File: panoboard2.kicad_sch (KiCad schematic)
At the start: 54 parts, among them J1 Conn_01x01, J10 Conn_01x01_Socket, J2 Conn_01x01_Socket, J3 Conn_01x01, J4 Conn_01x03, J5 I2C3, J7 Screw_Terminal_01x03, J8 Conn_01x08, J9 Conn_01x08_Pin, M1 Motor_AC, P1 Conn_WallPlug_Earth, P2 PCB_Patch, P3 PCB_Patch, SW1 SW_Push, SW2 SW_Push, U1 SRV05-4, U2 DS18B20, U8 OLED128X64

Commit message: More mods
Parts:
- added C1: 100n 250V, Capacitor_THT:C_Rect_L7.0mm_W6.0mm_P5.00mm, symbol Device:C
- added JP1, JP10, JP11, JP12, JP13, JP14, JP2, JP3, JP4, JP5, JP6, JP7, JP8, JP9: PCB_Pin_Breakout, TestPoint:TestPoint_Pad_1.0x1.0mm, symbol local:PCB_Pin_Breakout
- added M2: TINYPICO, TINYPICO:TINYPICO, symbol local:TINYPICO
- added R1: 22R 2W, Resistor_THT:R_Axial_DIN0207_L6.3mm_D2.5mm_P10.16mm_Horizontal, symbol Device:R
- added R3: 1k, Resistor_THT:R_Axial_DIN0207_L6.3mm_D2.5mm_P10.16mm_Horizontal, symbol Device:R
- added R4: 100k, Resistor_THT:R_Axial_DIN0207_L6.3mm_D2.5mm_P10.16mm_Horizontal, symbol Device:R
- J7: renamed from J8; value Conn_01x08 -> MOLEX 53375-0810
- RV1: renamed from RV3; value Varistor -> Varistor 10D271K
- U3: renamed from U1; now fitted
- renumbered D5 to D1, F3 to F2, J7 to J1, J4 to J2, J2 to J3, J10 to J4, J1 to J5, J3 to J6, J9 to J8, J5 to J9, JP9 to JP15, JP11 to JP16, JP13 to JP17, JP15 to JP18, JP17 to JP19, JP22 to JP20, JP24 to JP21, JP10 to JP22, JP12 to JP23, JP14 to JP24, JP16 to JP25, JP18 to JP26, JP20 to JP27, JP21 to JP28, JP23 to JP29, JP19 to JP30, JP1 to JP31, JP3 to JP32, JP5 to JP33, JP6 to JP34, JP8 to JP35, JP2 to JP36, JP4 to JP37, JP7 to JP38, R1 to R2, R24 to R5, U2 to U1, U8 to U2
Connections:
- net +3V3: now also U3.5 (VP), M2.7 (V3.3)
- net AC switcher 1/LOAD_A: now also C1.1
- net AC switcher 1/LOAD_N: now also R1.2
- net BUZZ1: now also JP27.1, U4.12 (A2CH0/TCH11/GPIO11), JP10.1, M2.14 (5), R3.2
- net BUZZ2: now also JP28.1, U4.14 (A2CH1/TCH12/GPIO12), JP11.1, M2.13 (18), R3.1, R4.2
- net DS18B20: now also U3.4 (IO3), JP4.1, M2.4 (15)
- net GND: now also U3.2 (VN), M2.9 (GND), R4.1
- net HEATER: now also U3.3 (IO2), JP3.1, M2.3 (27)
- net LED: now also JP19.1, U4.9 (A1CH8/TCH9/GPIO9), JP1.1, M2.1 (25)
- net MOTOR: now also U3.1 (IO1), JP2.1, M2.2 (26)
- net SCL: now also JP9.1, M2.15 (22)
- net SDA: now also JP8.1, M2.16 (21)
- net SW1: now also JP38.1, U4.20 (GPIO0), JP6.1, M2.6 (4); no longer JP27.1, U4.12 (A2CH0/TCH11/GPIO11)
- net SW2: now also JP26.1, U4.10 (A1CH9/TCH10/GPIO10), JP5.1, M2.5 (14); no longer JP28.1, U4.14 (A2CH1/TCH12/GPIO12)
- net THERM: now also U3.6 (IO4), JP14.1, M2.17 (32)
- net at M1.1: now also J8.8 (Pin_8); no longer J8.5 (Pin_5)
- net at M1.2: now also J8.5 (Pin_5); no longer J8.8 (Pin_8)
- net Earth: no longer names the net of J4.1 (Pin_1), P1.2 (AC_N)
- net Earth: no longer P1.3 (EARTH)
- new net: JP13.1, M2.11 (23)
- new net: JP12.1, M2.12 (19)
- new net: JP7.1, M2.18 (33)
- new net: C1.2, R1.1
- new net GNDPWR: P1.3 (EARTH)
- no-connect marks 7 -> 20
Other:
- sheet AC switcher renamed AC switcher 1
- sheet AC switcher1 renamed AC switcher 2
- note added: "Resistors are DNP"
- moved on the sheet: C2, J4, J6, J7, J8, M1, P2, P3, U4

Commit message: Revision 1.0c, after fit tests
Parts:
- removed JP10, JP11, JP12, JP13, JP14, JP15, JP16, JP17, JP18, JP19, JP2, JP20, JP21, JP26, JP27, JP28, JP3, JP35, JP36, JP37, JP38, JP4, JP5, JP6, JP7, JP8, JP9: PCB_Pin_Breakout, TestPoint:TestPoint_Pad_1.0x1.0mm, symbol local:PCB_Pin_Breakout
- added BZ2: FUET9018, Buzzer_Beeper:Buzzer_CUI_CPT-9019S-SMT, symbol Device:Buzzer
- added C3: 10n 1000V, Capacitor_THT:C_Rect_L18.0mm_W7.0mm_P15.00mm_FKS3_FKP3, symbol Device:C
- added C4: 10n, Capacitor_SMD:C_0805_2012Metric, symbol Device:C
- added D2: R LED, LED_SMD:LED_0805_2012Metric_Pad1.15x1.40mm_HandSolder, symbol Device:LED
- added D3: SS34, Diode_SMD:D_SMA, symbol Diode:SS34
- added H2: MountingHole, local:MountingHole, symbol local:MountingHole
- added J12: I2C2, Connector_PinHeader_2.54mm:PinHeader_1x04_P2.54mm_Vertical, symbol Connector_Generic:Conn_01x04
- added J4: Conn_01x01_Socket, symbol Connector:Conn_01x01_Socket
- added J7: WHT/HTR, TestPoint:TestPoint_Bridge_Pitch5.08mm_Drill1.3mm, symbol Connector_Generic:Conn_01x01
- added K1: Relay_SPDT, local:Relay_SPDT_SANYOU_SRD_Series_Form_C, symbol Relay:Relay_SPDT
- added Q1: 2N7000, Package_TO_SOT_THT:TO-92_Inline, symbol Transistor_FET:2N7000
- added Q2: BT136S-600, Package_TO_SOT_SMD:TO-252-2, symbol Triac_Thyristor:BT136-600
- added Q3: BT136-600, local:TO-220-3_Vertical, symbol Triac_Thyristor:BT136-600
- added R11: 220R, Resistor_SMD:R_0805_2012Metric, symbol Device:R
- added R12: 360R 1W, Resistor_THT:R_Axial_DIN0414_L11.9mm_D4.5mm_P15.24mm_Horizontal, symbol Device:R
- added R13: 360R, Resistor_THT:R_Axial_DIN0207_L6.3mm_D2.5mm_P10.16mm_Horizontal, symbol Device:R
- added R14: 10k, Resistor_SMD:R_0805_2012Metric, symbol Device:R
- added R4: 1k, Resistor_SMD:R_0805_2012Metric, symbol Device:R
- added R7: R so I=5mA, Resistor_SMD:R_0805_2012Metric, symbol Device:R
- added R8: R so I=10mA, Resistor_SMD:R_0805_2012Metric, symbol Device:R
- added R9: 39R 2W, Resistor_THT:R_Axial_DIN0617_L17.0mm_D6.0mm_P20.32mm_Horizontal, symbol Device:R
- added RV2, RV3, RV4, RV5: 10D271K, Varistor:RV_Disc_D12mm_W3.9mm_P7.5mm, symbol Device:Varistor
- added S1: JS1400BFQ, local:SW_JS1400BFQ, symbol local:JS1400BFQ
- added SW3, SW4, SW5: SW_Push, local:SW_Push_SPST_NO_432, symbol Switch:SW_Push
- added SW6: RotaryEncoder_Switch_MP, Rotary_Encoder:RotaryEncoder_Alps_EC11E-Switch_Vertical_H20mm, symbol Device:RotaryEncoder_Switch_MP
- added U6: MOC3063, Package_DIP:DIP-6_W7.62mm, symbol Relay_SolidState:MOC3063M
- added U7: MOC3063S, local:SOIC-6, symbol Relay_SolidState:MOC3063M
- BZ1: footprint (none) -> local:Buzzer_D12mm_H8.1mm; AliExpress (none) -> 1005006866915063; TODO (none) -> 1
- C1: footprint Capacitor_THT:C_Rect_L7.0mm_W6.0mm_P5.00mm -> Capacitor_THT:C_Rect_L9.0mm_W4.2mm_P7.50mm_MKT; AliExpress (none) -> 1005006719072774; TODO (none) -> 1
- C2: footprint Capacitor_THT:C_Rect_L41.5mm_W20.0mm_P37.50mm_MKS4 -> local:C_Rect_L24.0mm_W12.6mm_P20.00mm_MKT; AliExpress (none) -> 1005006292339527; TODO (none) -> 1
- D1: footprint (none) -> LED_SMD:LED_0805_2012Metric_Pad1.15x1.40mm_HandSolder; TODO (none) -> 1
- F2: value Fuse -> 5A; footprint (none) -> Fuse:Fuseholder_Cylinder-5x20mm_Stelvio-Kontek_PTF78_Horizontal_Open; AliExpress (none) -> 1005002077970716; TODO (none) -> ?
- H1: footprint ozhelm:MountingHole -> local:MountingHole
- J1: value Screw_Terminal_01x03 -> DS18B20; footprint (none) -> TerminalBlock_RND:TerminalBlock_RND_205-00046_1x03_P5.00mm_Horizontal; AliExpress (none) -> 32867118953
- J10: renamed from J8; value Conn_01x08_Pin -> MOTOR
- J11: renamed from J9; value I2C3 -> I2C1; symbol Connector_Generic:Conn_01x04 -> Connector_Generic_MountingPin:Conn_01x04_MountingPin; AliExpress (none) -> 1005005040794478; TODO (none) -> 1
- J2: value Conn_01x03 -> THERMISTOR; footprint (none) -> Connector_JST:JST_EH_B3B-EH-A_1x03_P2.50mm_Vertical; TODO (none) -> 1
- J3: AliExpress (none) -> 33040947135; TODO (none) -> 1
- J5: renamed from J4; AliExpress (none) -> 33040947135; TODO (none) -> 1
- J6: renamed from J5; value Conn_01x01 -> BLK/MAINS L; footprint (none) -> TestPoint:TestPoint_Bridge_Pitch5.08mm_Drill1.3mm; AliExpress (none) -> 1005005477459338; TODO (none) -> 1
- J8: renamed from J6; value Conn_01x01 -> ORA/MAINS N; footprint (none) -> TestPoint:TestPoint_Bridge_Pitch5.08mm_Drill1.3mm; AliExpress (none) -> 1005005477459338; TODO (none) -> 1
- J9: renamed from J7; footprint Connector_PinHeader_2.54mm:PinHeader_1x08_P2.54mm_Vertical -> local:MOLEX_533750810; AliExpress (none) -> 1005006639933927; TODO (none) -> ?
- M2: footprint TINYPICO:TINYPICO -> local:TINYPICO; TODO (none) -> 1
- P2, P3: footprint ozhelm:SolderJumper-2_P1.3mm_Bridged_Pad1.0x1.5mm -> local:SolderJumper-2_P1.3mm_Bridged_Pad1.0x1.5mm; TODO (none) -> 1
- PS1: value IRM-03-3.3 -> HLK-5M03; footprint Converter_ACDC:Converter_ACDC_MeanWell_IRM-03-xx_THT -> Converter_ACDC:Converter_ACDC_Hi-Link_HLK-5Mxx; symbol Converter_ACDC:IRM-03-3.3 -> Converter_ACDC:HLK-5M03; AliExpress (none) -> 1005006490570335; TODO (none) -> 1
- R2: renamed from R1; footprint Resistor_THT:R_Axial_DIN0207_L6.3mm_D2.5mm_P10.16mm_Horizontal -> local:R_Axial_DIN0516_L15.5mm_D5.0mm_P22.2mm_Horizontal
- R3: renamed from R5; footprint (none) -> Resistor_SMD:R_0805_2012Metric
- R5: renamed from R3; footprint Resistor_THT:R_Axial_DIN0207_L6.3mm_D2.5mm_P10.16mm_Horizontal -> Resistor_SMD:R_0805_2012Metric
- R6: renamed from R4; footprint Resistor_THT:R_Axial_DIN0207_L6.3mm_D2.5mm_P10.16mm_Horizontal -> Resistor_SMD:R_0805_2012Metric
- RV1: value Varistor 10D271K -> 10D271K; footprint (none) -> Varistor:RV_Disc_D12mm_W3.9mm_P7.5mm; TODO (none) -> 1
- SW1, SW2: footprint (none) -> local:SW_Push_SPST_NO_432; LCSC (none) -> C255812; TODO (none) -> 1
- U1: AliExpress (none) -> 1005007018104116
- U2: renamed from U3; symbol Power_Protection:SRV05-4 -> local:SRV05-4; TODO (none) -> 1
- U3: renamed from U4; value ~ -> M5STAMP-S3; footprint (none) -> local:STAMP-S3-DIP_copy
- U4: renamed from U2; footprint (none) -> local:128x64OLED; AliExpress (none) -> 1005006373062872
- renumbered R2 to R1
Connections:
- net AC switcher 2/LOAD_A is gone; now on an unnamed net: R1.1
- net +3V3: now also J1.3 (Pin_3), PS1.4 (+Vout), U4.2 (VCC), D3.1 (K), J12.2 (Pin_2), K1.A1; no longer J1.1 (Pin_1), PS1.16 (+Vo), U4.8 (VDD)
- net BUZZ1: now also M2.13 (18), R4.2; no longer BZ1.1 (+), M2.14 (5), R5.2
- net BUZZ2: now also M2.14 (5), BZ2.2 (-); no longer M2.13 (18)
- net DS18B20: now also JP1.1, M2.3 (27), U3.5 (A1CH4/TCH5/GPIO5); no longer M2.4 (15), U3.7 (A1CH6/TCH7/GPIO7)
- net GND: now also J1.1 (Pin_1), PS1.3 (-Vout), R3.2, SW1.2, U4.1 (GND), C4.2, J12.1 (Pin_1), Q1.1 (S), R14.1, R7.1, S1.5, S1.SH1, S1.SH2, SW3.2, SW4.1, SW5.1, SW6.C, SW6.MP, SW6.S2, U6.2, U7.2; no longer D1.1 (K), J1.3 (Pin_3), PS1.14 (-Vo), SW1.1, U4.4 (VSS)
- net HEATER: now also M2.2 (26), U3.3 (A1CH2/TCH3/GPIO3), R11.1; no longer M2.3 (27), U3.5 (A1CH4/TCH5/GPIO5)
- net LED: now also D1.2 (A), M2.18 (33), U3.26 (GPIO43/CLK1/TXD); no longer JP1.1, M2.1 (25), R3.1, U3.9 (A1CH8/TCH9/GPIO9)
- net MAINS_A: now also P3.1, RV3.1, RV5.1
- net MAINS_N: now also C1.1, PS1.2 (AC/N), C3.2, K1.11, Q2.1 (A1), Q3.1 (A1), R13.2, RV2.1, RV4.1; no longer PS1.3 (AC/N)
- net MOTOR: now also M2.4 (15), U2.6 (IO4), U3.7 (A1CH6/TCH7/GPIO7), D2.2 (A), R8.1; no longer M2.2 (26), U2.1 (IO1), U3.3 (A1CH2/TCH3/GPIO3)
- net SCL: now also U3.15 (A2CH2/TCH13/GPIO13/SDA), U4.3 (SCL), J12.4 (Pin_4); no longer U3.17 (A2CH4/TCH1/GPIO15/SCL), U4.6 (SCL)
- net SDA: now also U3.17 (A2CH4/TCH1/GPIO15/SCL), U4.4 (SDA), J12.3 (Pin_3); no longer U3.15 (A2CH2/TCH13/GPIO13/SDA), U4.7 (SDA)
- net SW1: now also M2.11 (23), SW1.1, U3.19 (GPIO39/CLK3/MTCK), S1.2, SW6.S1; no longer M2.6 (4), SW1.2, U3.20 (GPIO0)
- net SW2: now also M2.12 (19), U3.20 (GPIO0), S1.4, SW6.A; no longer M2.5 (14), U3.10 (A1CH9/TCH10/GPIO10)
- net THERM: now also U2.1 (IO1), U3.24 (GPIO44/CLK2/RXD); no longer U2.6 (IO4), U3.1 (A1CH0/TCH1/GPIO1)
- net AC switcher 1/LOAD_A renamed MTR_N
- net MTR_N: now also R2.2, Q2.2 (A2), Q3.2 (A2), R12.1, RV2.2, RV3.2; no longer C1.1
- removed net AC switcher 1/LOAD_N: P3.1, R2.2
- net AC switcher 2/LOAD_N: no longer names the net of R1.2
- net AC switcher 2/LOAD_N: now also J4.1 (Pin_1)
- new net: Q2.3 (G), Q3.3 (G), R13.1, U6.4, U7.4
- new net: C4.1, R8.2, U6.1, U7.1
- new net: Q1.2 (G), R11.2, R14.2
- new net: D1.1 (K), R3.1
- new net: BZ1.1 (+), BZ2.1 (+), R4.1, R5.2
- new net: C3.1, R9.2
- new net: D3.2 (A), K1.A2, Q1.3 (D)
- new net: D2.1 (K), R7.2
- new net: R12.2, U6.6, U7.6
- new net HTR_N: J7.1 (Pin_1), K1.14, R9.1, RV4.2, RV5.2
- new net SW3: M2.1 (25), S1.3, SW3.1, SW6.B, U3.1 (A1CH0/TCH1/GPIO1)
- new net SW4: M2.5 (14), S1.1, SW4.2, U3.9 (A1CH8/TCH9/GPIO9)
- new net SW5: M2.6 (4), S1.6, SW5.2, U3.10 (A1CH9/TCH10/GPIO10)
- no-connect marks 20 -> 21
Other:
- removed sheet AC switcher 1
- removed sheet AC switcher 2
- note added: "https://electronics.stackexchange.com/questions/248743/how-is-the-gate-trigger-resistor-value-calculated-for-a-triac/248775#248775"
- note added: "https://pdf1.alldatasheet.com/datasheet-pdf/view/5043/MOTOROLA/MOC3063.html"
- title: (none) -> Panoboard2
- moved on the sheet: BZ1, C1, C2, D1, F1, F2, J1, J10, J2, J3, J5, J6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

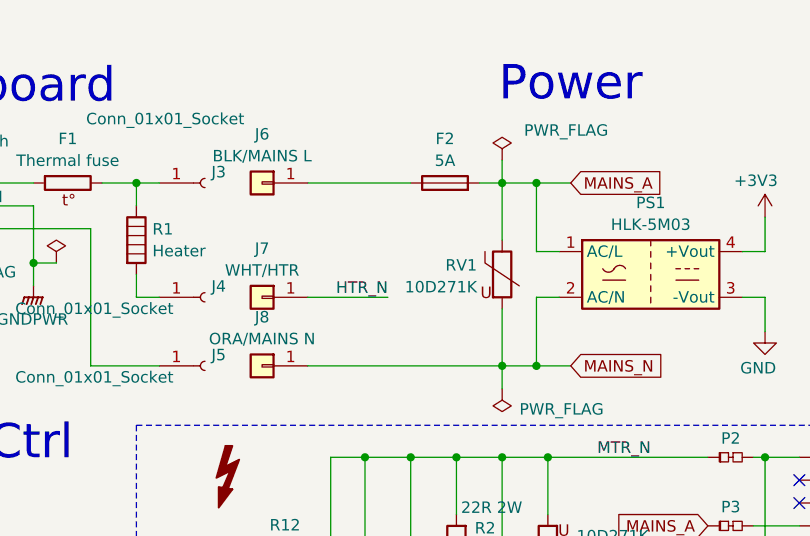
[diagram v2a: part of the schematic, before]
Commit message: Many improvements
Moved fuse to the neutral line so heater is protected
Added slot under R2
Moved mounting hole
Improved board outline
Added OSHW licence and KiCad shout-out
Fixed buzzer pin pitch
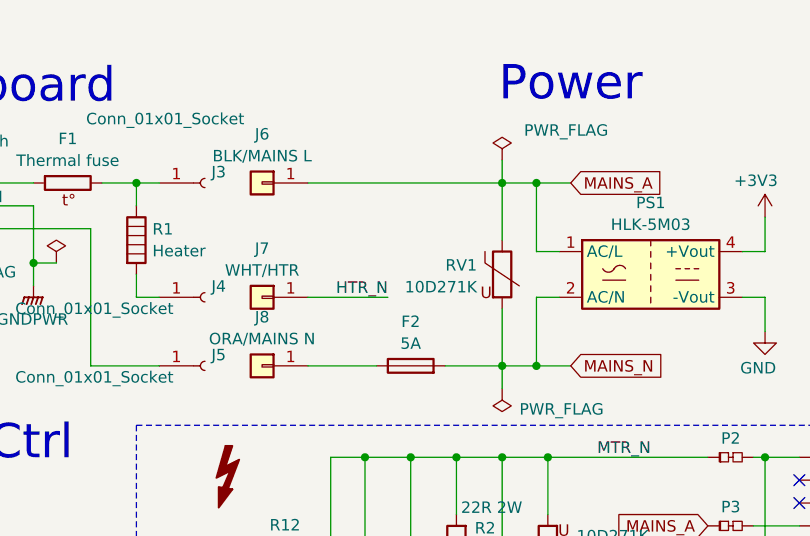
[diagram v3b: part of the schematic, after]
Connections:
- net MAINS_A: now also J6.1 (Pin_1); no longer F2.2
- net MAINS_N: now also F2.2; no longer J8.1 (Pin_1)
- net at F2.1: now also J8.1 (Pin_1); no longer J6.1 (Pin_1)
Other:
- moved on the sheet: F2
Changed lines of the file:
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@@
 	(wire
 		(pts
-			(xy 76.2 30.48) (xy 87.63 30.48)
+			(xy 76.2 30.48) (xy 97.79 30.48)
 		)
 		(stroke
@@
 	(wire
 		(pts
-			(xy 76.2 50.8) (xy 97.79 50.8)
+			(xy 76.2 50.8) (xy 83.82 50.8)
 		)
 		(stroke
@@
 	(wire
 		(pts
+			(xy 91.44 50.8) (xy 97.79 50.8)
+		)
+		(stroke
+			(width 0)
+			(type default)
+		)
+	)
+	(wire
+		(pts
 			(xy 76.2 146.05) (xy 90.17 146.05)
 		)
@@
 	(wire
 		(pts
-			(xy 95.25 30.48) (xy 97.79 30.48)
-		)
-		(stroke
-			(width 0)
-			(type default)
-		)
-	)
-	(wire
-		(pts
 			(xy 146.05 68.58) (xy 146.05 73.66)
 		)
@@
 	(symbol
 		(lib_id "Device:Fuse")
-		(at 91.44 30.48 90)
+		(at 87.63 50.8 90)
 		(unit 1)
 		(exclude_from_sim no)
@@
 		(fields_autoplaced yes)
 		(property "Reference" "F2"
-			(at 91.44 25.5735 90)
+			(at 87.63 45.8935 90)
 			(effects
 				(font
@@
 		)
 		(property "Value" "5A"
-			(at 91.44 27.9978 90)
+			(at 87.63 48.3178 90)
 			(effects
 				(font
@@
 		)
 		(property "Footprint" "Fuse:Fuseholder_Cylinder-5x20mm_Stelvio-Kontek_PTF78_Horizontal_Open"
-			(at 91.44 32.258 90)
+			(at 87.63 52.578 90)
 			(effects
 				(font
@@
 		)
 		(property "Datasheet" "~"
-			(at 91.44 30.48 0)
+			(at 87.63 50.8 0)
 			(effects
 				(font
@@
 		)
 		(property "Description" "Fuse"
-			(at 91.44 30.48 0)
+			(at 87.63 50.8 0)
 			(effects
 				(font
@@
 		)
 		(property "TODO" "?"
-			(at 91.44 30.48 0)
+			(at 87.63 50.8 0)
 			(effects
 				(font
@@
 		)
 		(property "AliExpress" "1005002077970716"
-			(at 91.44 30.48 0)
+			(at 87.63 50.8 0)
 			(effects
 				(font

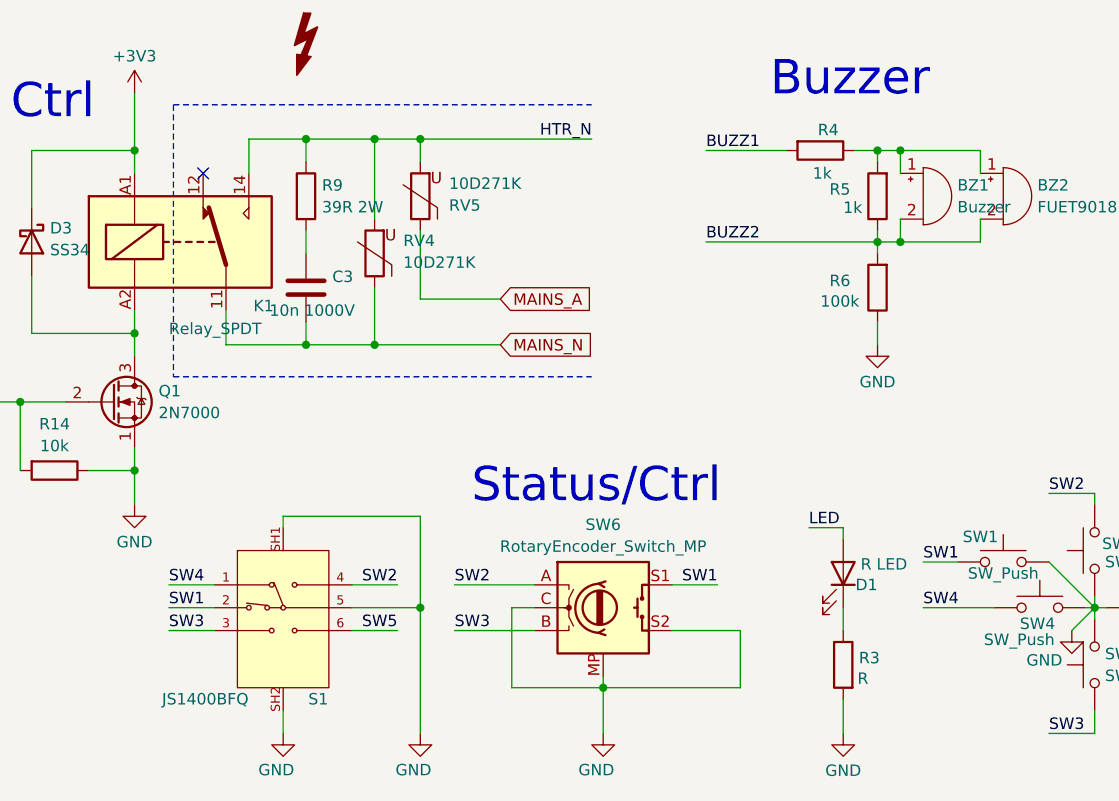
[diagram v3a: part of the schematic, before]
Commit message: Rotated incorrectly placed motor connector, and added many 3D models.
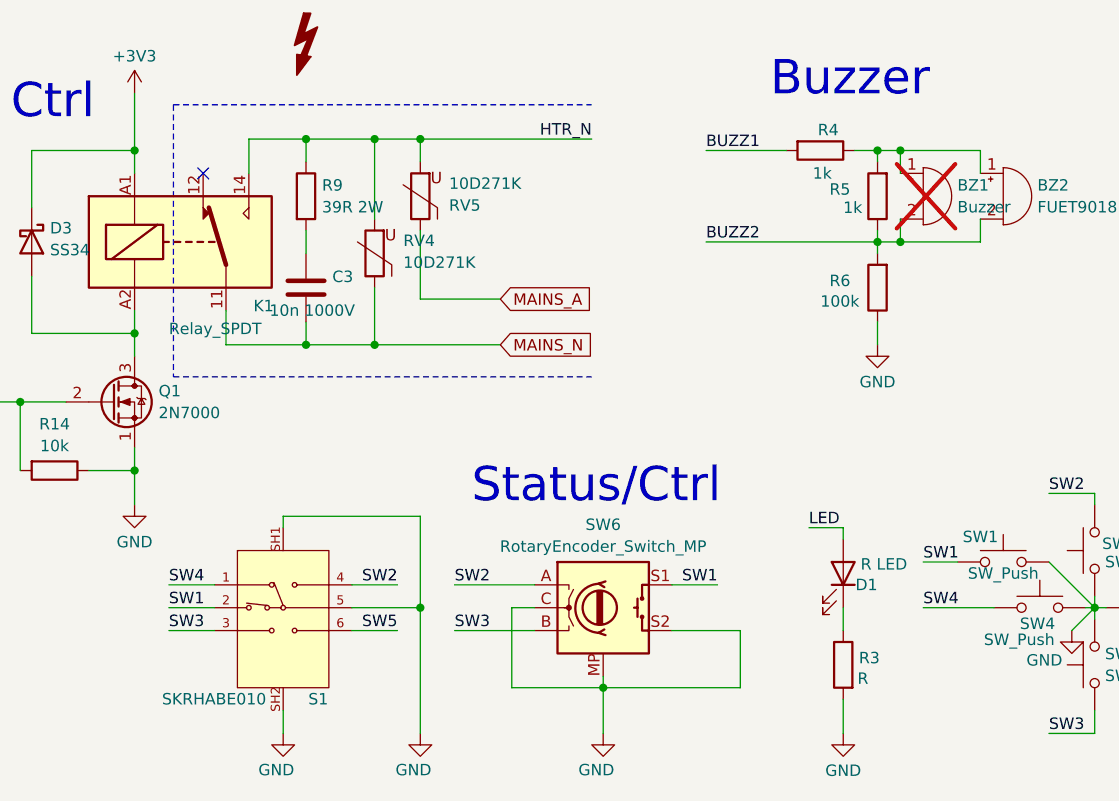
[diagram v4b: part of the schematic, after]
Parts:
- BZ1: now not fitted
- J11: LCSC (none) -> C160404
- J6, J7, J8: footprint TestPoint:TestPoint_Bridge_Pitch5.08mm_Drill1.3mm -> local:TE-1742361-1-QC-Tab
- Q3: LCSC C5455738 -> C916534
- S1: value JS1400BFQ -> SKRHABE010; footprint local:SW_JS1400BFQ -> local:SKRHABE010; LCSC (none) -> C139794
- SW1, SW2, SW3, SW4, SW5: LCSC C255812 -> C707339
- SW6: LCSC (none) -> C143799
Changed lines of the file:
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@@
 			)
 		)
-		(property "LCSC" "C5455738"
+		(property "LCSC" "C916534"
 			(at 87.63 76.2 0)
 			(effects
@@
 			)
 		)
-		(property "LCSC" "C255812"
+		(property "LCSC" "C707339"
 			(at 162.56 175.26 0)
 			(effects
@@
 			)
 		)
-		(property "LCSC" "C255812"
+		(property "LCSC" "C707339"
 			(at 156.21 181.61 0)
 			(effects
@@
 			)
 		)
-		(property "Footprint" "TestPoint:TestPoint_Bridge_Pitch5.08mm_Drill1.3mm"
+		(property "Footprint" "local:TE-1742361-1-QC-Tab"
 			(at 71.12 43.18 0)
 			(effects
@@
 			)
 		)
-		(property "Datasheet" "~"
+		(property "Datasheet" "https://www.digikey.com/en/products/detail/te-connectivity-amp-connectors/1742361-1/2308741"
 			(at 71.12 43.18 0)
 			(effects
@@
 			)
 		)
-		(property "LCSC" "C255812"
+		(property "LCSC" "C707339"
 			(at 156.21 168.91 0)
 			(effects
@@
 			)
 		)
-		(property "Footprint" "TestPoint:TestPoint_Bridge_Pitch5.08mm_Drill1.3mm"
+		(property "Footprint" "local:TE-1742361-1-QC-Tab"
 			(at 71.12 50.8 0)
 			(effects
@@
 			)
 		)
-		(property "Datasheet" "~"
+		(property "Datasheet" "https://www.digikey.com/en/products/detail/te-connectivity-amp-connectors/1742361-1/2308741"
 			(at 71.12 50.8 0)
 			(effects
@@
 			)
 		)
-		(property "Footprint" "TestPoint:TestPoint_Bridge_Pitch5.08mm_Drill1.3mm"
+		(property "Footprint" "local:TE-1742361-1-QC-Tab"
 			(at 71.12 30.48 0)
 			(effects
@@
 			)
 		)
-		(property "Datasheet" "~"
+		(property "Datasheet" "https://www.digikey.com/en/products/detail/te-connectivity-amp-connectors/1742361-1/2308741"
 			(at 71.12 30.48 0)
 			(effects
@@
 			)
 		)
-		(property "Value" "JS1400BFQ"
+		(property "Value" "SKRHABE010"
 			(at 52.578 185.42 0)
 			(effects
@@
 			)
 		)
-		(property "Footprint" "local:SW_JS1400BFQ"
+		(property "Footprint" "local:SKRHABE010"
 			(at 102.108 189.484 0)
 			(effects
@@
 			)
 		)
+		(property "LCSC" "C139794"
+			(at 66.04 177.8 0)
+			(effects
+				(font
+					(size 1.27 1.27)
+				)
+				(hide yes)
+			)
+		)
 		(pin "SH2"
 		)
@@
 			)
 		)
-		(property "LCSC" "C255812"
+		(property "LCSC" "C707339"
 			(at 150.114 175.26 0)
 			(effects
@@
 			)
 		)
+		(property "LCSC" "C160404"
+			(at 171.45 142.24 0)
+			(effects
+				(font
+					(size 1.27 1.27)
+				)
+				(hide yes)
+			)
+		)
 		(pin "2"
 		)
@@
 			)
 		)
-		(property "LCSC" "C255812"
+		(property "LCSC" "C707339"
 			(at 146.05 170.18 0)
 			(effects
@@
 		(in_bom yes)
 		(on_board yes)
-		(dnp no)
+		(dnp yes)
 		(fields_autoplaced yes)
 		(property "Reference" "BZ1"
@@
 			(at 101.6 175.26 0)
 			(effects
+				(font
+					(size 1.27 1.27)
+				)
+				(hide yes)
+			)
+		)
+		(property "LCSC" "C143799"
+			(at 101.6 175.26 0)
+			(effects

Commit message: Added LCSC part number for 2N7000
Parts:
- Q1: LCSC (none) -> C8545
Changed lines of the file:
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@@
+			)
+		)
+		(property "LCSC" "C8545"
+			(at 46.99 152.4 0)
+			(effects
+				(font
+					(size 1.27 1.27)
+				)
+				(hide yes)
 			)
 		)
